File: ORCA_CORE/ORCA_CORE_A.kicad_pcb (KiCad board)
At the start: 2 copper layers, 218 x 99 mm, 201 parts, among them J1 Vext_in, J10 Raspberry_Pi_2_3, J11 wheel_left, J12 md_out, J13 md_out, J14 limit_sw_upper, J15 limit_sw_upper, J16 limit_sw_under, J17 data_line_power, J18 +6V_motor, J19 +5Vin_cpu, J2 6Vout, J20 limit_sw_under, J21 Vin_motor, J22 Vin_motor, J23 md_arm, J24 md_fork, J25 servo_arm, J26 Vin_motor, J3 6Vout, J31 I2C_1, J32 I2C_2, J33 cpu_female_left, J34 cpu_female_right, J35 hat_male_right, J36 enable_arm, J37 enable_arm, J38 servo_arm, J39 md_arm, J4 6Vout, J40 md_fork, J41 cpu_male_left, J42 uart, J43 uart_device, J44 servo_camera, J45 reset, J46 reset, J47 led, J48 led, J49 USB_B_Micro, J5 6Vin, J50 USB_A, J51 usb_A_device, J52 usb_A, J53 cover_left, J54 base_left, J55 servo connectors, J59 base_right, J6 Vext_out, J60 cover_right, J7 6Vout, J8 wheel_front, J9 wheel_right, P1 USB_C_Receptacle_USB2.0, Q1 BSS138, Q2 BSS138, Q3 TJ60S04M3L, Q8 BSS138, SW2 REST_sw, U1 FT230XS, U10 TLP293, U11 TLP293, U12 TLP293, U13 TLP293, U14 BNO055, U15 TLP293, U16 TLP293, U17 AZ1117-3.3, U18 TLP293, U19 TLP293, U2 PCA9685PW_Q900_118, U20 TLP293, U21 TLP293, U22 AZ1117-3.3, U23 TLP293, U24 TLP293, U25 TLP293, U26 PMW3360, U3 AM2837, U4 AM2837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

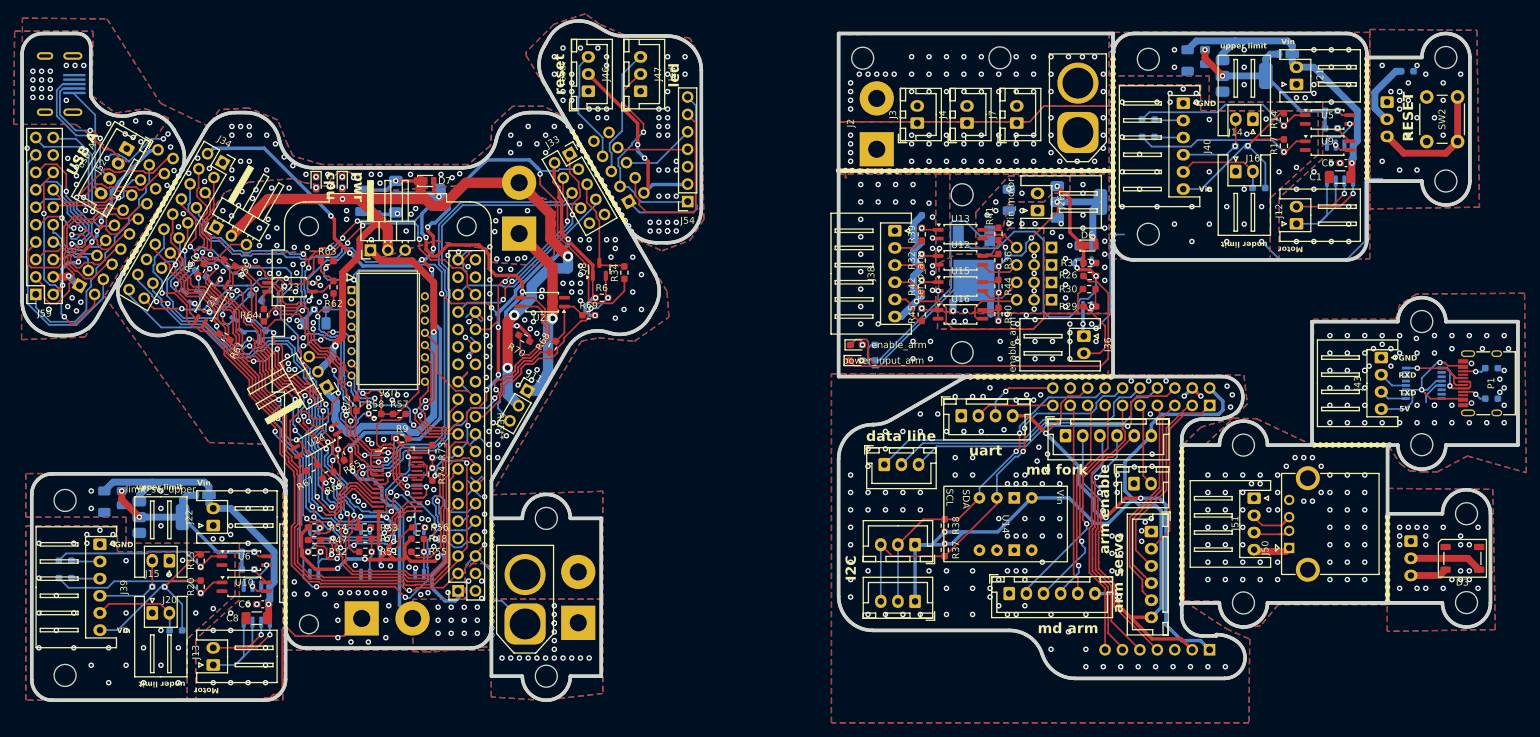
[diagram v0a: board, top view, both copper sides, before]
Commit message: correct few errors in usp
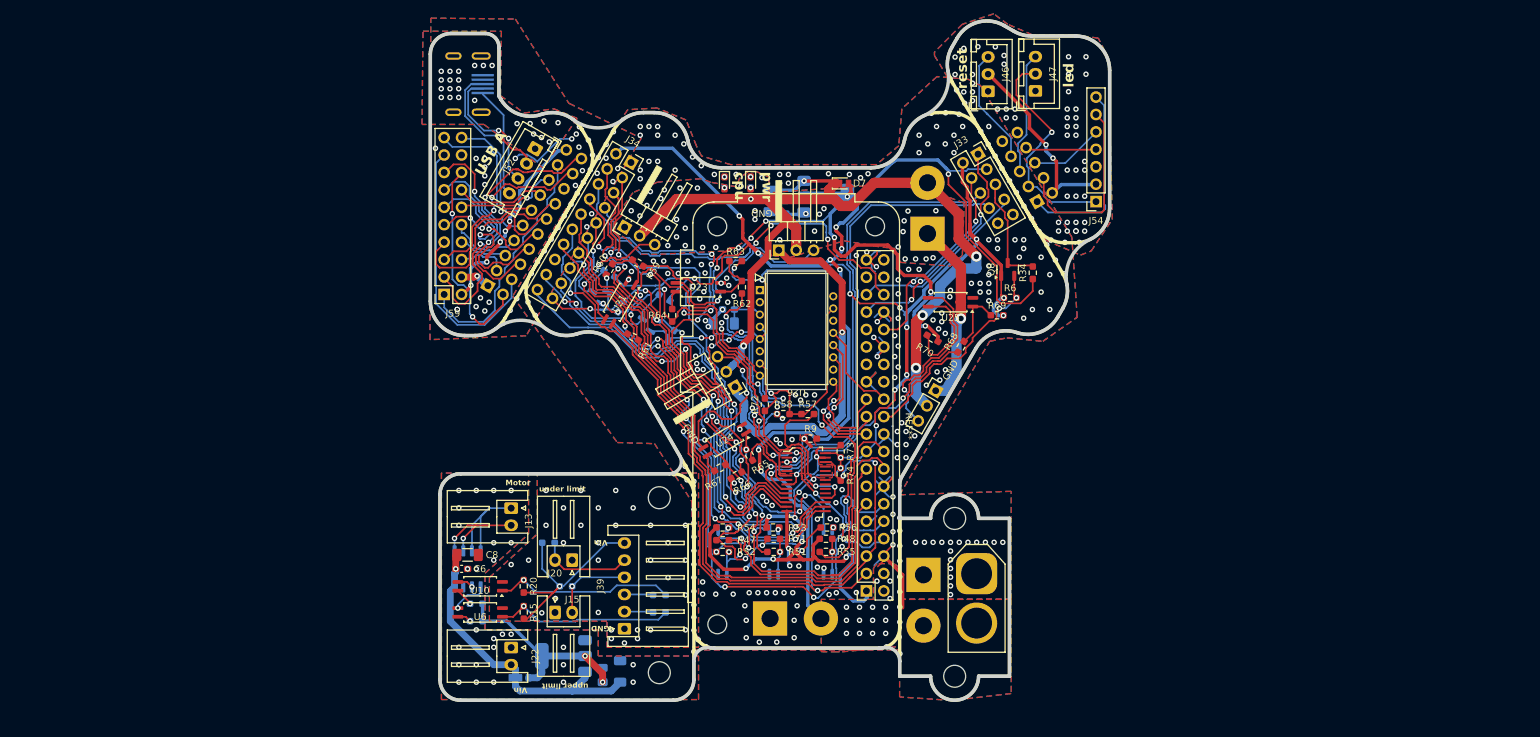
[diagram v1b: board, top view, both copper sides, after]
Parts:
- removed C1, C9: 10u/50V, Capacitor_SMD:C_1206_3216Metric_Pad1.33x1.80mm_HandSolder
- removed C10, C2: 22u25V, Capacitor_SMD:C_0805_2012Metric_Pad1.18x1.45mm_HandSolder
- removed C5: 0.1u, Capacitor_SMD:C_0603_1608Metric_Pad1.08x0.95mm_HandSolder
- removed C7: 220u, Capacitor_SMD:C_1206_3216Metric_Pad1.33x1.80mm_HandSolder
- removed D1, D6: CUHS20560, Diode:Diode_US2H
- removed D3: WS2812B, LED_SMD:LED_WS2812B_PLCC4_5.0x5.0mm_P3.2mm
- removed D4: enable_arm, LED_SMD:LED_0603_1608Metric_Pad1.05x0.95mm_HandSolder
- removed D5: power_input_arm, LED_SMD:LED_0603_1608Metric_Pad1.05x0.95mm_HandSolder
- removed H1, H2: Hole_uart, MountingHole:MountingHole_3.2mm_M3
- removed H11, H12: Hole_Vhub, MountingHole:MountingHole_3.2mm_M3
- removed H13, H14: Hole_md, MountingHole:MountingHole_3.2mm_M3
- removed H23, H24: Hole_usbA, MountingHole:MountingHole_3.2mm_M3
- removed H25, H26: Hole_arm, MountingHole:MountingHole_3.2mm_M3
- removed H3, H4: Hole_led, MountingHole:MountingHole_3.2mm_M3
- removed H5, H6: Hole_reset, MountingHole:MountingHole_3.2mm_M3
- removed J12: md_out, Connector_JST:JST_XH_S2B-XH-A_1x02_P2.50mm_Horizontal
- removed J14: limit_sw_upper, Connector_JST:JST_XH_S2B-XH-A_1x02_P2.50mm_Horizontal
- removed J16: limit_sw_under, Connector_JST:JST_XH_S2B-XH-A_1x02_P2.50mm_Horizontal
- removed J17: data_line_power, Connector_JST:JST_XH_B3B-XH-A_1x03_P2.50mm_Vertical
- removed J2: 6Vout, Conn:power_pad
- removed J21, J26: Vin_motor, Connector_JST:JST_XH_S2B-XH-A_1x02_P2.50mm_Horizontal
- removed J23: md_arm, Connector_JST:JST_XH_B6B-XH-A_1x06_P2.50mm_Vertical
- removed J24: md_fork, Connector_JST:JST_XH_B6B-XH-A_1x06_P2.50mm_Vertical
- removed J25: servo_arm, Connector_JST:JST_XH_B6B-XH-A_1x06_P2.50mm_Vertical
- removed J3, J4, J7: 6Vout, Connector_JST:JST_XH_B2B-XH-A_1x02_P2.50mm_Vertical
- removed J31: I2C_1, Connector_JST:JST_XH_B3B-XH-A_1x03_P2.50mm_Vertical
- removed J32: I2C_2, Connector_JST:JST_XH_B3B-XH-A_1x03_P2.50mm_Vertical
- removed J36: enable_arm, Connector_JST:JST_XH_S2B-XH-A_1x02_P2.50mm_Horizontal
- removed J37: enable_arm, Connector_JST:JST_XH_B2B-XH-A_1x02_P2.50mm_Vertical
- removed J38: servo_arm, Connector_JST:JST_XH_S6B-XH-A_1x06_P2.50mm_Horizontal
- removed J40: md_fork, Connector_JST:JST_XH_S6B-XH-A_1x06_P2.50mm_Horizontal
- removed J42: uart, Connector_JST:JST_XH_B4B-XH-A_1x04_P2.50mm_Vertical
- removed J43: uart_device, Connector_JST:JST_XH_S4B-XH-A_1x04_P2.50mm_Horizontal
- removed J45: reset, Connector_JST:JST_XH_B3B-XH-A_1x03_P2.50mm_Vertical
- removed J48: led, Connector_JST:JST_XH_B3B-XH-A_1x03_P2.50mm_Vertical
- removed J5: 6Vin, Conn:AMASS_XT60_Vertifcal_withmodel_female
- removed J50: USB_A, Conn:TypeA_connector_KUSBX-AS1N-B
- removed J51: usb_A_device, Connector_JST:JST_XH_S4B-XH-A_1x04_P2.50mm_Horizontal
- removed J53: cover_left, Connector_PinHeader_2.54mm:PinHeader_1x07_P2.54mm_Vertical
- removed J55: servo connectors, Conn:PinHeader_03x04_P2.54mm_Vertical
- removed J60: cover_right, Connector_PinHeader_2.54mm:PinHeader_2x10_P2.54mm_Vertical
- removed P1: USB_C_Receptacle_USB2.0, Conn:USB_C_Receptacle_XKB_U262-16XN-4BVC11
- removed Q3: TJ60S04M3L, toshiba:2-7M1A
- removed R1: 560, Resistor_SMD:R_0603_1608Metric_Pad0.98x0.95mm_HandSolder
- removed R10, R16, R29, R32, R39, R42, R45: 100, Resistor_SMD:R_0603_1608Metric_Pad0.98x0.95mm_HandSolder
- removed R12, R14, R17, R18, R22, R24, R30, R33, R36, R37, R38, R40, R41, R43, R44, R46, R50: 2.2k, Resistor_SMD:R_0603_1608Metric_Pad0.98x0.95mm_HandSolder
- removed R2, R3: 5.1k, Resistor_SMD:R_0603_1608Metric_Pad0.98x0.95mm_HandSolder
- removed R26: 10k, Resistor_SMD:R_0603_1608Metric_Pad0.98x0.95mm_HandSolder
- removed R27, R28: 1k, Resistor_SMD:R_0603_1608Metric_Pad0.98x0.95mm_HandSolder
- removed R31: 47, Resistor_SMD:R_0603_1608Metric_Pad0.98x0.95mm_HandSolder
- removed SW2: REST_sw, Button_Switch_THT:SW_PUSH_6mm
- removed U1: FT230XS, Package_SO:SSOP-16_3.9x4.9mm_P0.635mm
- removed U11, U12, U13, U15, U16, U5, U9: TLP293, Package_SO:SOIC-4_4.55x2.6mm_P1.27mm
- removed U14: BNO055, IMU:BNO055
- removed U17, U7: AZ1117-3.3, Package_TO_SOT_SMD:SOT-223-3_TabPin2
- removed U3: AM2837, Package_SO:SOP-8_3.9x4.9mm_P1.27mm
- moved H16 90.4 mm to (130.9, 110.0), turned to 0 degrees
- moved H15 90.2 mm to (130.9, 135.5), turned to 180 degrees
- moved R11 86.9 mm to (130.9, 126.7), turned to 0 degrees
- moved R19 86.6 mm to (130.9, 124.2), turned to 0 degrees
- moved C3 79.1 mm to (125.2, 135.3), turned to 90 degrees
- moved J39 77.4 mm to (125.8, 129.1), turned to 90 degrees
- moved C4 74.7 mm to (122.6, 135.8), turned to 90 degrees
- moved J1 65.6 mm to (177.0, 124.9), turned to -90 degrees
- moved U8 62.1 mm to (116.9, 133.1), turned to 180 degrees
- moved J20 61.7 mm to (118.2, 119.1), turned to 180 degrees
- moved D7 60.4 mm to (157.2, 64.2)
- moved C13 59.5 mm to (140.9, 82.6)
- moved D19 59.5 mm to (140.4, 64.1)
- moved D8 59.5 mm to (144.2, 64.1)
- moved G*** 59.5 mm to (150.6, 105.5)
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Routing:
- net Vin_3V3_cpu_hat: track 182.1 -> 57.6 mm, vias 10 -> 7
- net GND1: track 208.7 -> 107.1 mm, vias 738 -> 363
- net +3V3: track 398.8 -> 328.3 mm, vias 43 -> 34
- net Vin_cpu_hat: track 129.8 -> 64.0 mm, vias 6 -> 3
- net GND: track 146.7 -> 85.5 mm, vias 113 -> 64
- net Net-(J31-Pin_3): track 59.3 -> 0.00 mm, vias 2 -> 0
- net Vin_arm: track 51.4 -> 0.00 mm, vias 1 -> 0
- net Net-(J31-Pin_2): track 50.6 -> 0.00 mm, vias 2 -> 0
- net +6V_in: track 44.5 -> 0.00 mm, vias 6 -> 0
- net Net-(J17-Pin_3): track 43.8 -> 0.00 mm, vias 1 -> 0
- net +6V: track 227.1 -> 183.6 mm, vias 8 -> 7
- net Net-(Q3-G): track 43.4 -> 0.00 mm, vias 2 -> 0
- net Net-(J17-Pin_2): track 43.0 -> 0.00 mm
- net Net-(J17-Pin_1): track 43.0 -> 0.00 mm
- net /cpu_hat/IN_A_fork_out: track 36.2 -> 0.00 mm, vias 1 -> 0
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- removed copper zone on B.Cu, net +6V_in
- removed copper zone on F.Cu, net +6V_in
- removed copper zone on B.Cu, net +6V_out
- removed copper zone on F.Cu, net +6V_out
- removed copper zone on B.Cu, net Net-(J2-Pin_2)
- removed copper zone on F.Cu, net Net-(J2-Pin_2)
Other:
- board size 218 x 99 mm -> 99 x 99 mm
- board text removed: "3V3"
- board text removed: "I2C"
- board text removed: "RESET"
- board text removed: "RXD"
- board text removed: "SCL"
- board text removed: "SDA"
- board text removed: "TXD"
- board text removed: "arm enable"
- board text removed: "arm servo"
- board text removed: "checker"
- board text removed: "data line"
- board text removed: "detector"
- board text removed: "limit_sw_under"
- board text removed: "md arm"
- board text removed: "md fork"
- board text removed: "order"
- board text removed: "uart"
